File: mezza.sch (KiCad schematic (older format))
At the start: 27 parts, among them CON1 USB-MINI-B, P1 CONN_02X20, P2 CONN_02X20, U2 FT230XS

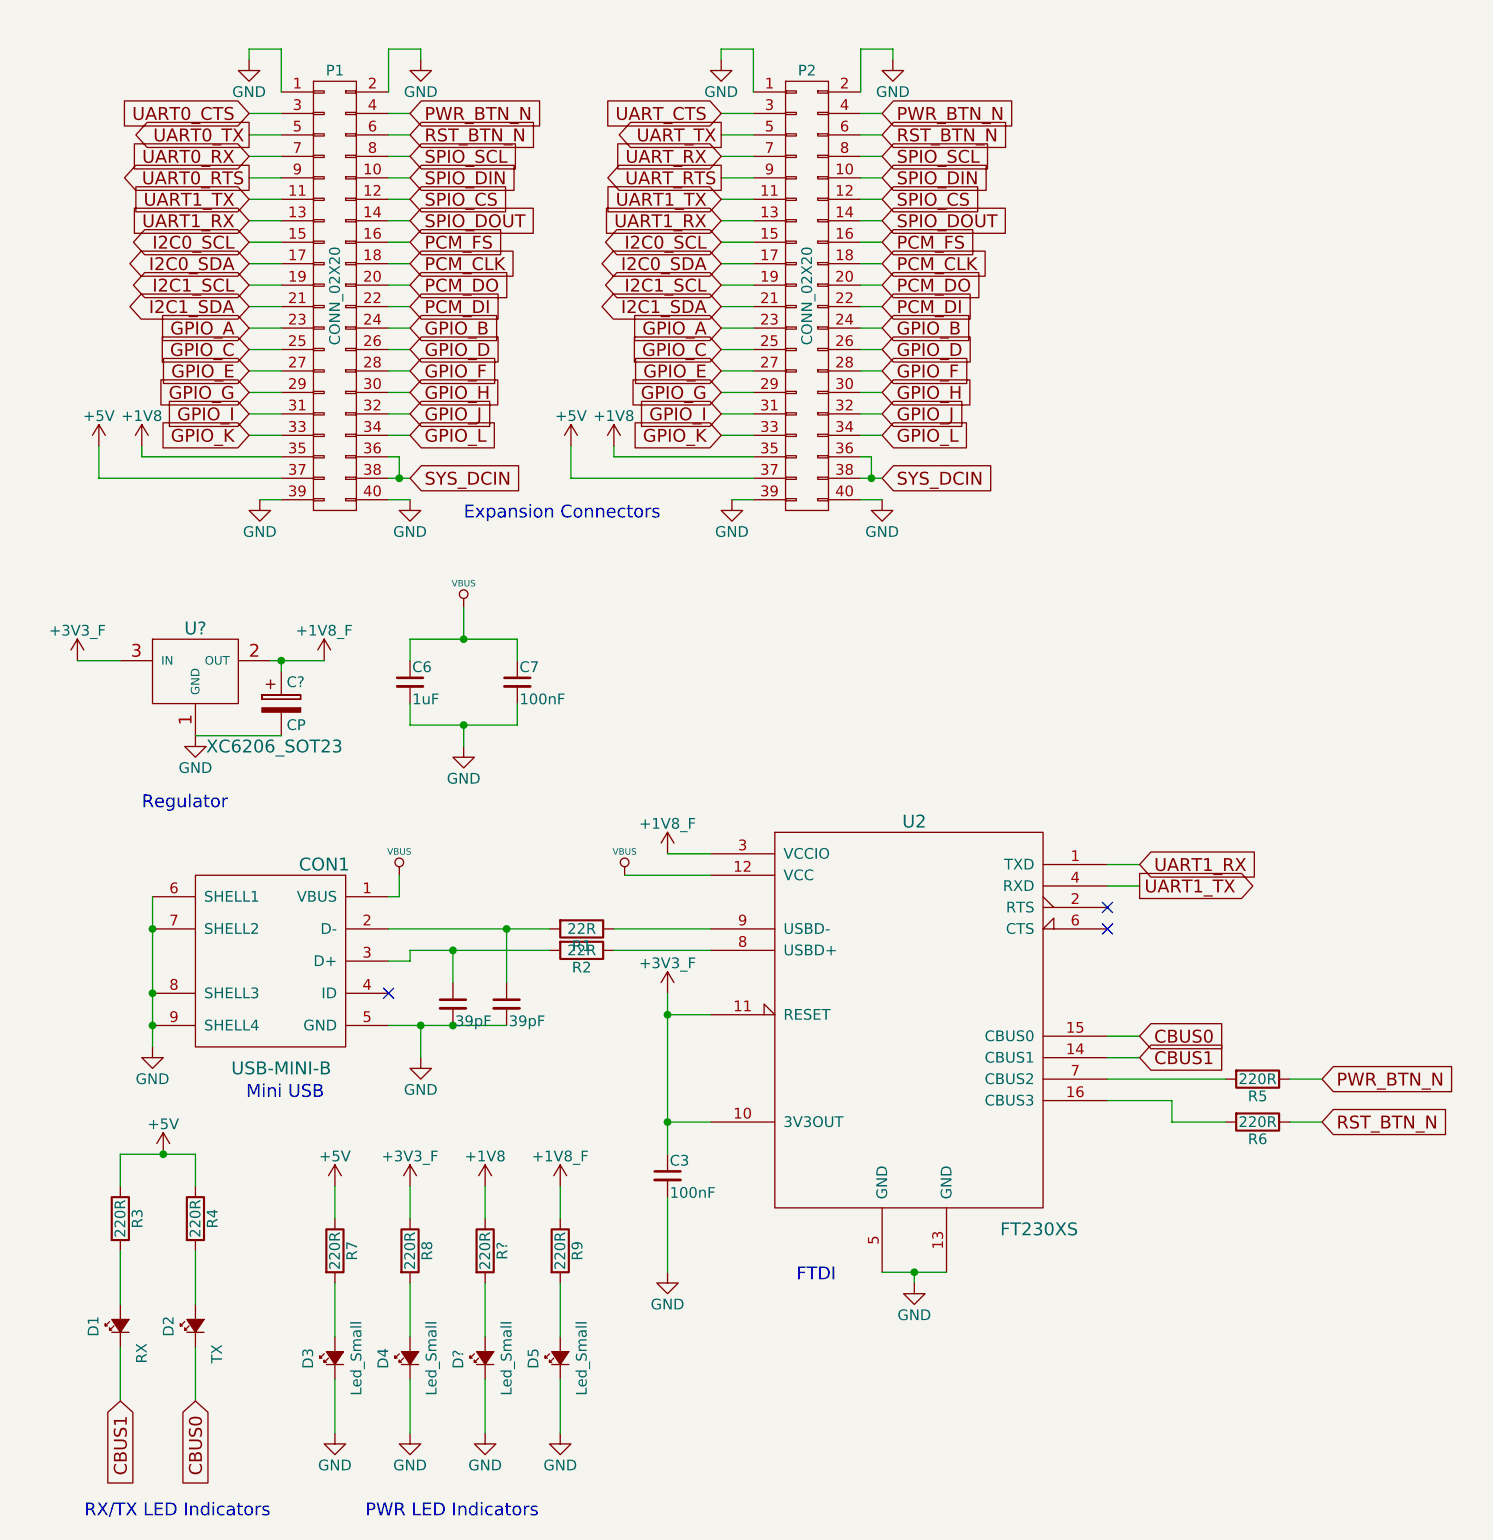
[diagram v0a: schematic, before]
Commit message: Tidy Up Project
Unneeded footprints have been removed from the project.
The footprint folder has been renamed (stop kicad complaining).
Readme.md has been updated to mathch the project.

Signed-off-by: Sophie Haynes <sophie.haynes@linao.org>
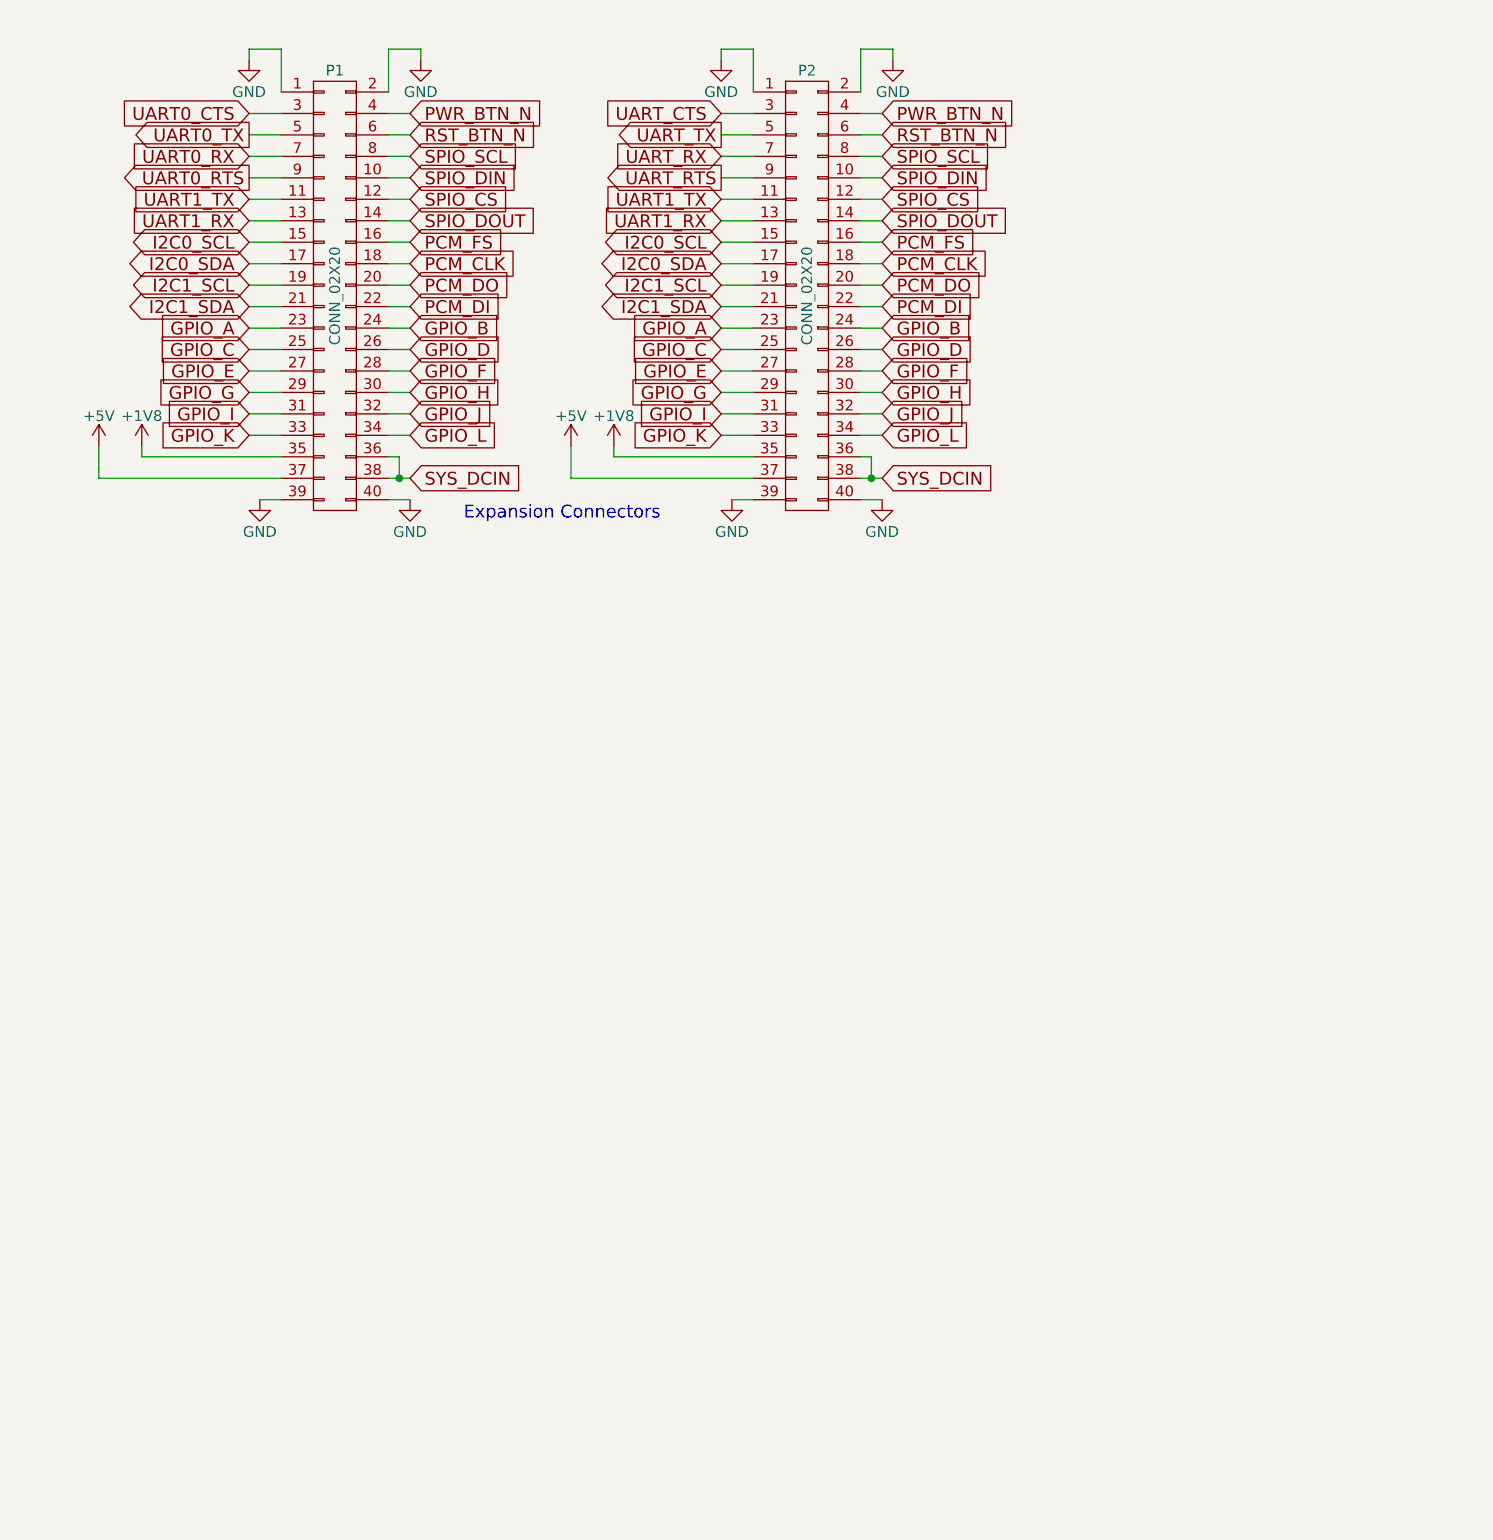
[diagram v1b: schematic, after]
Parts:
- removed C3, C7: 100nF, Capacitors_SMD:C_0603, symbol C_Small
- removed C4, C5: 39pF, Capacitors_SMD:C_0603, symbol C_Small
- removed C6: 1uF, Capacitors_SMD:C_0603, symbol C_Small
- removed C?: CP, symbol CP
- removed CON1: USB-MINI-B, mezza:USB_MICRO_B_ST-USB-001E, symbol USB-MINI-B
- removed D1: RX, symbol Led_Small
- removed D2: TX, symbol Led_Small
- removed D3, D4, D5, D?: Led_Small, symbol Led_Small
- removed R1, R2: 22R, mezza:R_0603_Seeed, symbol R
- removed R3, R4, R5, R6, R7, R8, R9, R?: 220R, symbol R
- removed U2: FT230XS, mezza:SSOP-16_3.9x4.9mm_Pitch0.635mm_Seeed, symbol FT230XS
- removed U?: XC6206_SOT23, mezza:SOT-23_Seeed, symbol XC6206_SOT23
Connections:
- no-connect marks 3 -> 0
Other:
- note removed: "FTDI"
- note removed: "Mini USB"
- note removed: "PWR LED Indicators"
- note removed: "RX/TX LED Indicators"
- note removed: "Regulator"

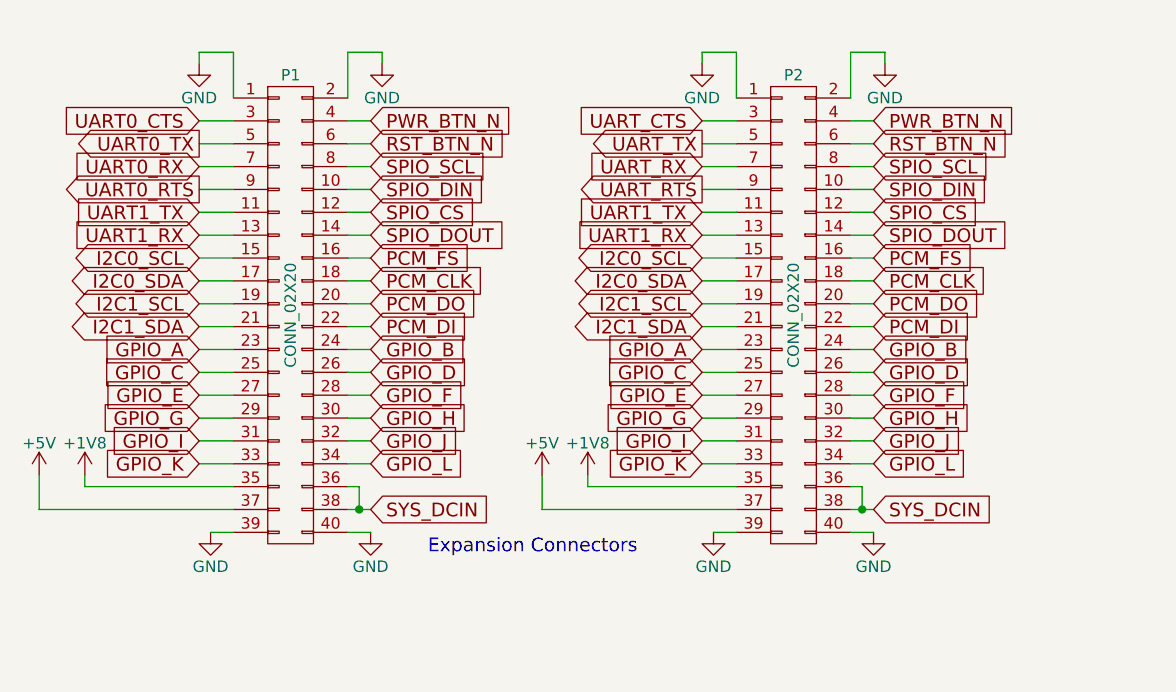
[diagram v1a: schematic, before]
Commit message: Annotate Connector in Schematic
The second connector in the schematic has been annoted to inform users who
wish to use a through hole connector instead, to delete that connector.
The correct footprints have been assigned too.

Signed-off-by: Sophie Haynes <sophie.haynes@linaro.org>
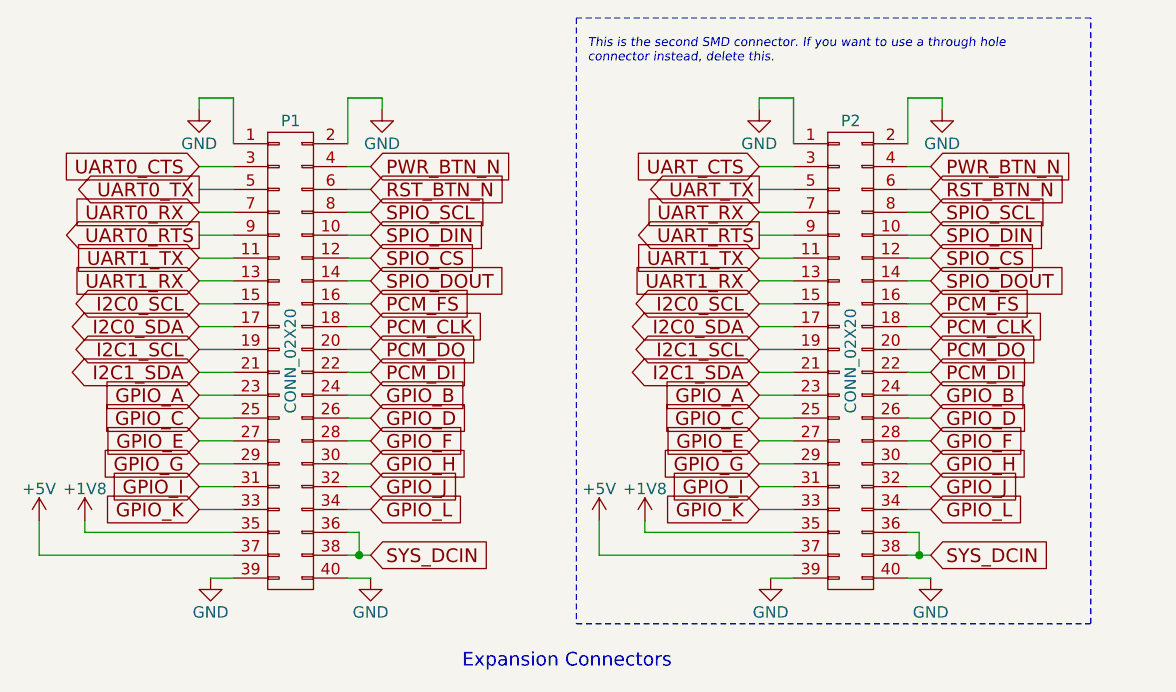
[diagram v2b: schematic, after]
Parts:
- P1: footprint mezza:Socket_Strip_SMD_2x20_Pitch2mm -> 96boards:Socket_Strip_SMD_2x20_Pitch2mm
- P2: footprint (none) -> 96boards:Pin_Header_SMD_2x20_Pitch2mm
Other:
- note added: "This is the second SMD connector. If you want to use a through hole \nconnector instead, delete this.\n"
- moved on the sheet: P1, P2
